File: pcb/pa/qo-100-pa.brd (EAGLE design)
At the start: 75 x 48 mm, 45 parts, among them CON1 2EDG-2P, Q1 BLP9G0722-20G, U1 ADP7142AUJZ, U2 2450BP15E0100

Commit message: Lots of changes PCBs in production Stencil in production Added and changed simulation files
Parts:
- C10, C17: value 20pF -> 12pF
- C13, C15: value 12pF -> 2.2pF
- C19, C8: value 43pF -> 47pF
- C21, C7: value 62pF -> 100pF
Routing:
- net N$7: track 0.03 -> 3.60 mm
- net N$4: track 37.8 -> 35.3 mm
- net AUTO_BIAS_EN: track 36.6 -> 38.4 mm
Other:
- board text added: "DC IN Max. 28 V"
- board text added: "IcyRadio PA v1 May 2020"
- board text added: "RF IN +30 dBm"
- board text added: "RF OUT +43 dBm"

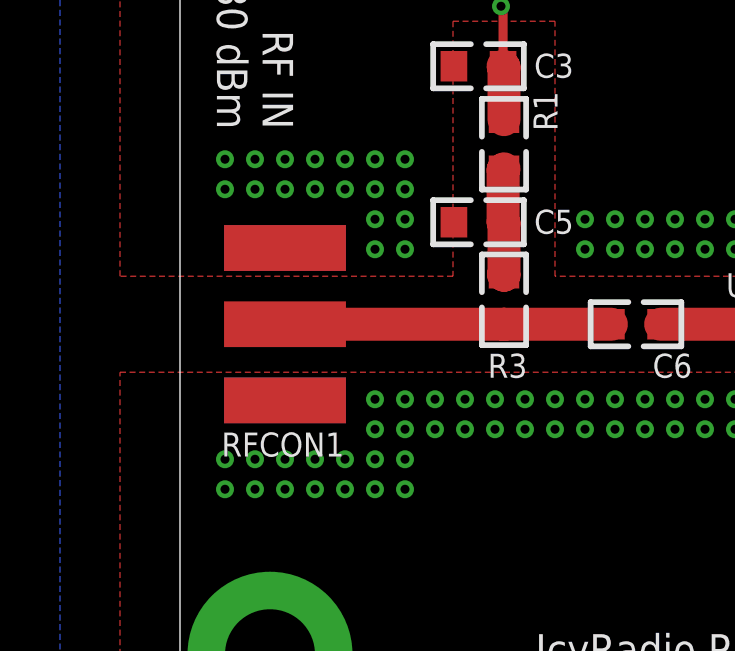
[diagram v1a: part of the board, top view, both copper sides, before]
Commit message: Added LNB controller schematic and PCB Added GPSDO schematic Added example firmware
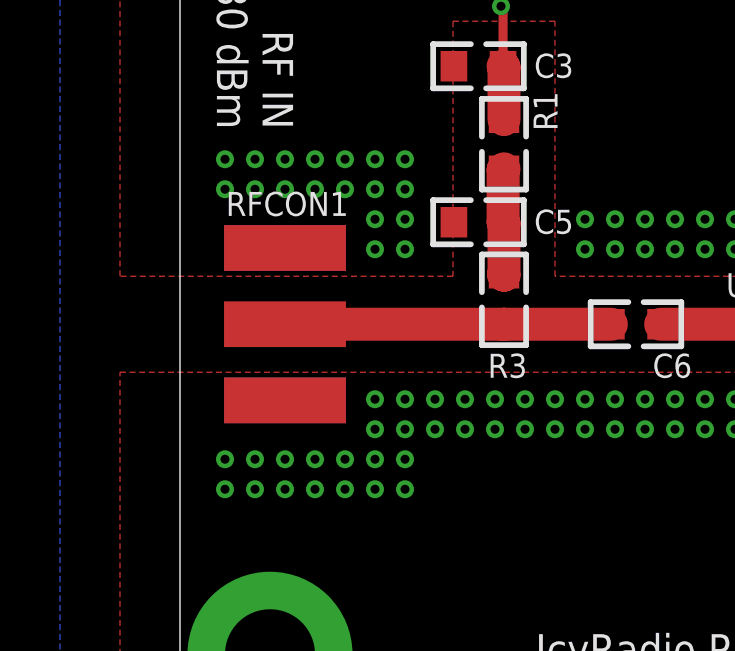
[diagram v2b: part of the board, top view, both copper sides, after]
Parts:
- turned RFCON1 to 270 degrees
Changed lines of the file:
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@@
 <?xml version="1.0" encoding="utf-8"?>
 <!DOCTYPE eagle SYSTEM "eagle.dtd">
-<eagle version="9.5.2">
+<eagle version="9.6.1">
 <drawing>
 <settings>
@@
 <attribute name="VALUE" x="34.732" y="17.4456" size="0.8" layer="27" font="vector" ratio="10" rot="SR90" align="center-left"/>
 </element>
-<element name="RFCON1" library="RF Connector" package="SMA-EDGE" value="RFCON-SMA-EDGE" x="3.5" y="14" smashed="yes" rot="R90">
-<attribute name="NAME" x="5.47" y="9.99" size="0.8" layer="25" font="vector" ratio="10" rot="R180" align="center-left"/>
+<element name="RFCON1" library="RF Connector" package="SMA-EDGE" value="RFCON-SMA-EDGE" x="3.5" y="14" smashed="yes" rot="R270">
+<attribute name="NAME" x="1.53" y="18.01" size="0.8" layer="25" font="vector" ratio="10" align="center-left"/>
 </element>
 <element name="RFCON2" library="RF Connector" package="SMA-EDGE" value="RFCON-SMA-EDGE" x="71.5" y="14" smashed="yes" rot="R90">

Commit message: Matched PA to 2.4 GHz
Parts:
- C12: value 0.5pF -> 2.2pF
- C16: value 2.2pF -> 0.5pF
- C18: value 1.8pF -> 1.2pF
- C22: value 1.2pF -> DNP
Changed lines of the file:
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@@
 <attribute name="VOLTAGE" value="" x="81.49" y="99.88" size="1.778" layer="27" rot="R90" display="off"/>
 </element>
-<element name="C12" library="Capacitor" package="CAP0603" value="0.5pF" x="24.8" y="13.18" smashed="yes" rot="R270">
+<element name="C12" library="Capacitor" package="CAP0603" value="2.2pF" x="24.8" y="13.18" smashed="yes" rot="R270">
 <attribute name="NAME" x="23.8736" y="15.416" size="0.8" layer="25" font="vector" ratio="10" rot="SR0" align="center-left"/>
 <attribute name="VALUE" x="22.768" y="16.1264" size="0.8" layer="27" font="vector" ratio="10" rot="SR270" align="center-left"/>
@@
 <attribute name="VOLTAGE" value="" x="42.94" y="-43.15" size="1.778" layer="27" display="off"/>
 </element>
-<element name="C16" library="Capacitor" package="CAP0603" value="2.2pF" x="49.3" y="18.9" smashed="yes" rot="R90">
+<element name="C16" library="Capacitor" package="CAP0603" value="0.5pF" x="49.3" y="18.9" smashed="yes" rot="R90">
 <attribute name="NAME" x="49.284" y="20.7536" size="0.8" layer="25" font="vector" ratio="10" rot="SR90" align="center-left"/>
 <attribute name="VALUE" x="51.332" y="15.9536" size="0.8" layer="27" font="vector" ratio="10" rot="SR90" align="center-left"/>
@@
 <attribute name="VOLTAGE" value="50V" x="72.62" y="4.59" size="1.778" layer="27" display="off"/>
 </element>
-<element name="C18" library="Capacitor" package="CAP0603" value="1.8pF" x="49.3" y="9.1" smashed="yes" rot="R270">
+<element name="C18" library="Capacitor" package="CAP0603" value="1.2pF" x="49.3" y="9.1" smashed="yes" rot="R270">
 <attribute name="NAME" x="49.284" y="5.4536" size="0.8" layer="25" font="vector" ratio="10" rot="SR90" align="center-left"/>
 <attribute name="VALUE" x="47.268" y="12.0464" size="0.8" layer="27" font="vector" ratio="10" rot="SR270" align="center-left"/>
@@
 <attribute name="VOLTAGE" value="" x="85.76" y="-43.15" size="1.778" layer="27" display="off"/>
 </element>
-<element name="C22" library="Capacitor" package="CAP0603" value="1.2pF" x="53.4" y="13.18" smashed="yes" rot="R270">
+<element name="C22" library="Capacitor" package="CAP0603" value="DNP" x="53.4" y="13.18" smashed="yes" rot="R270">
 <attribute name="NAME" x="52.4736" y="15.416" size="0.8" layer="25" font="vector" ratio="10" rot="SR0" align="center-left"/>
 <attribute name="VALUE" x="51.368" y="16.1264" size="0.8" layer="27" font="vector" ratio="10" rot="SR270" align="center-left"/>

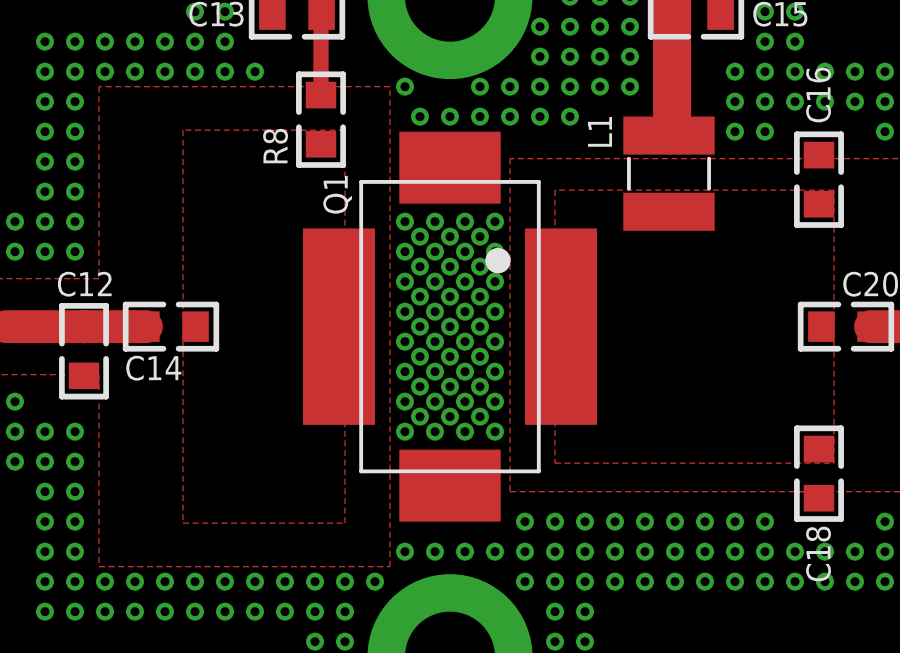
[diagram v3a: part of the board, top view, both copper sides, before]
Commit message: Changed PA package to include bottom exposed pad Enlarged PA PCB exposed GND on the bottom side to improve heat transfer
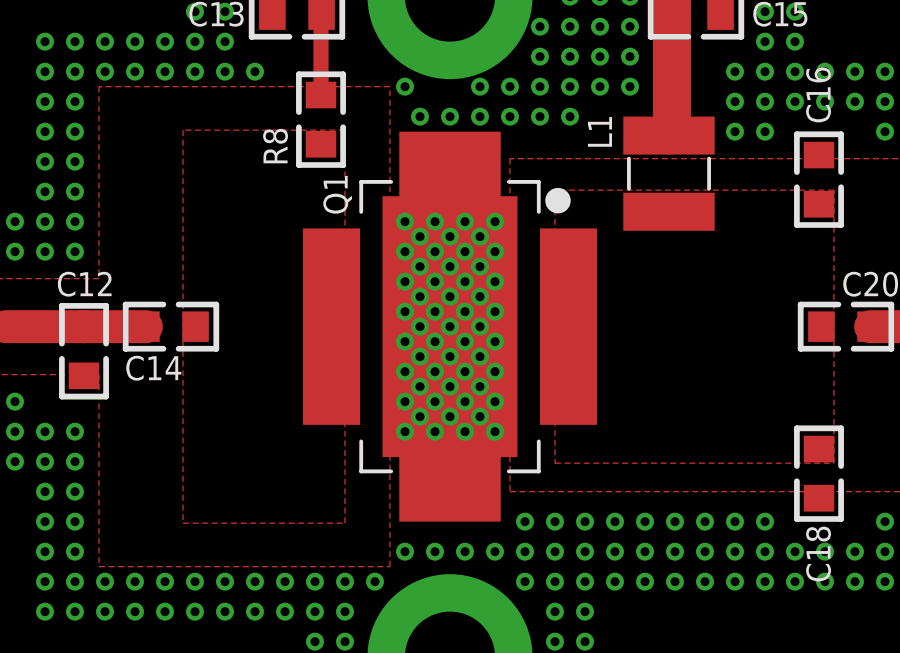
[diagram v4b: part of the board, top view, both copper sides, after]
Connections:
- net GND: now also Q1.3@2
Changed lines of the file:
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@@
 <drawing>
 <settings>
-<setting alwaysvectorfont="no"/>
+<setting alwaysvectorfont="yes"/>
 <setting verticaltext="up"/>
 </settings>
@@
 <text x="16.5" y="2.4" size="1.016" layer="21" font="vector" ratio="12" rot="SR0" align="center">IcyRadio PA v1
 May 2020</text>
-<rectangle x1="35" y1="9" x2="39" y2="19" layer="30"/>
+<rectangle x1="30" y1="7" x2="44" y2="21" layer="30"/>
 </plain>
 <attributes>
@@
 <via x="40" y="26" extent="1-16" drill="0.3"/>
 <via x="36" y="28" extent="1-16" drill="0.3"/>
+<contactref element="Q1" pad="3@2"/>
 </signal>
 <signal name="N$2">
@@
 <mfgpreviewcolor name="substratecolor" color="0xFF786E46"/>
 </mfgpreviewcolors>
+<errors>
+</errors>
 </board>
 </drawing>

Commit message: Update 2EDG library on PA
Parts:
- CON1: value 2EDG-2P -> 2EDG-2P-5.08MM; device Generic Connector:2EDG-2P -> Generic Connector:2EDG-2P-5.08MM
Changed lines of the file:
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@@
 <drawing>
 <settings>
-<setting alwaysvectorfont="yes"/>
+<setting alwaysvectorfont="no"/>
 <setting verticaltext="up"/>
 </settings>
@@
 <attribute name="VOLTAGE" value="" x="-8.74" y="78.27" size="1.778" layer="27" rot="R180" display="off"/>
 </element>
-<element name="CON1" library="Generic Connector" package="2EDG-2P" value="2EDG-2P" x="55" y="36" smashed="yes" rot="R90">
+<element name="CON1" library="Generic Connector" package="2EDG-2P-5.08MM" value="2EDG-2P-5.08MM" x="55" y="36" smashed="yes" rot="R90">
 <attribute name="NAME" x="52.3" y="31" size="0.8" layer="25" font="vector" ratio="10" rot="R90" align="center-left"/>
 </element>
